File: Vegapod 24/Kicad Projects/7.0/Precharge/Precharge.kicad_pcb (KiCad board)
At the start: 2 copper layers, 92.5 x 97 mm, 53 parts, among them J1 VCU, J2 E-Stop, J3 LV Supply, J4 Intertial Switch, J5 Contactor1, J6 DCV, J7 Contactor2, J8 24V IN, K1 Relay_SPDT, K2 Relay_SPDT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

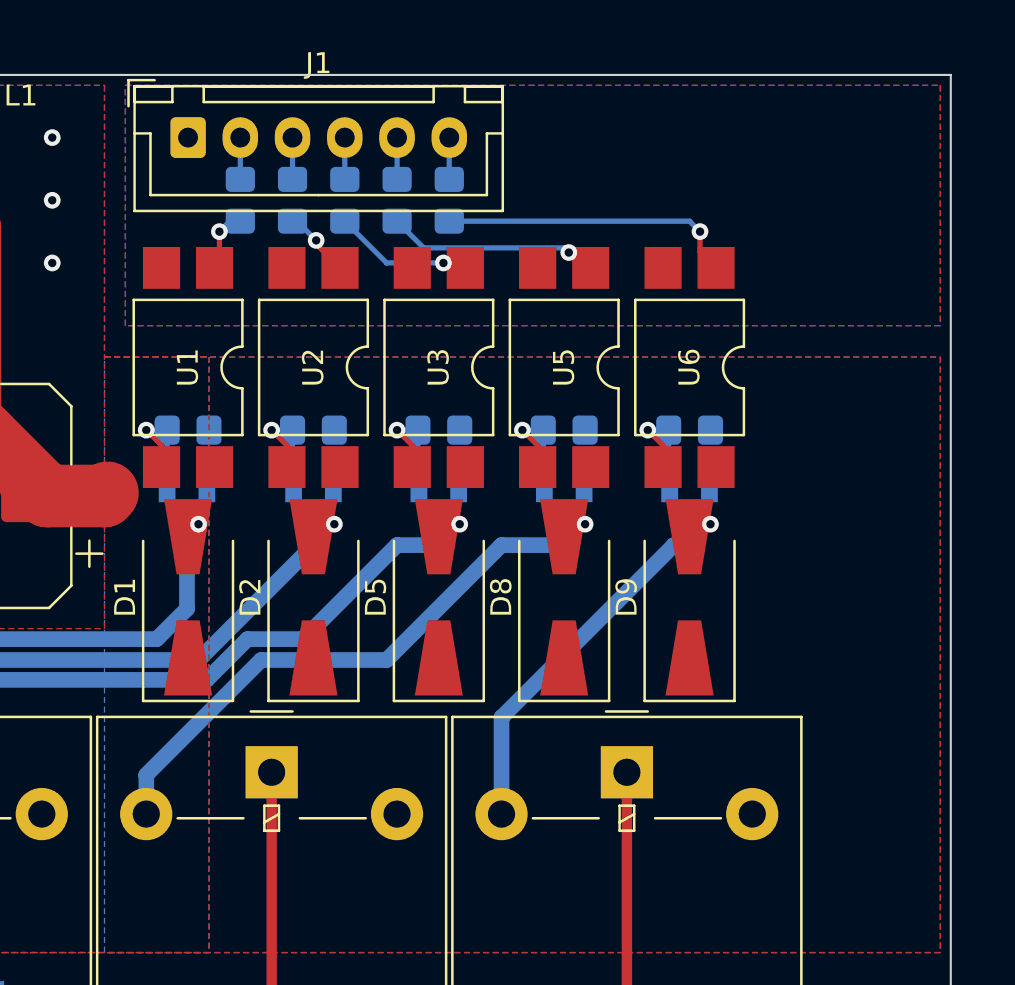
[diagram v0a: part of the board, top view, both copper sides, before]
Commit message: Added IMD Support to interlock
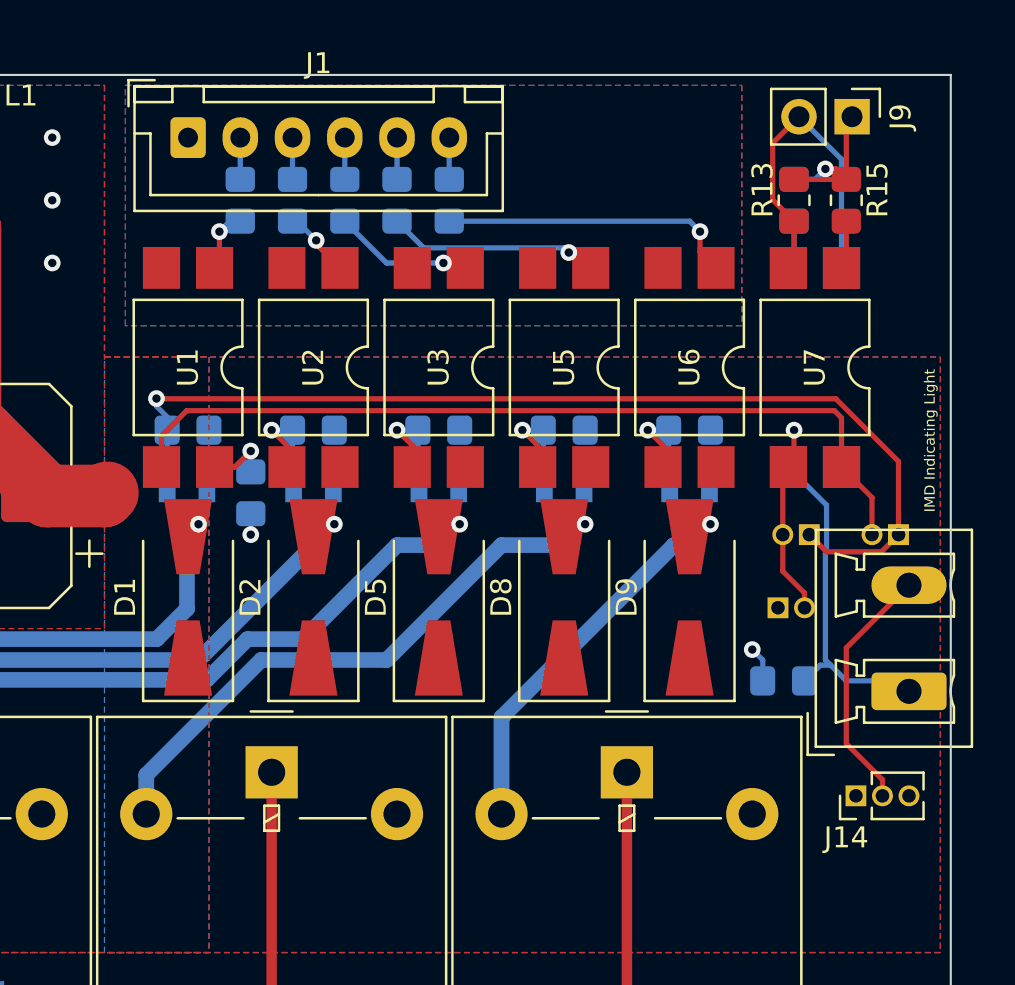
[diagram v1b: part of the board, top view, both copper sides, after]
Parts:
- added J10: ISO165Jumper, Connector_PinHeader_1.27mm:PinHeader_1x02_P1.27mm_Vertical, B.Cu at (127.0, 35.0)
- added J11: ISO165Jumper, Connector_PinHeader_1.27mm:PinHeader_1x02_P1.27mm_Vertical, B.Cu at (121.2, 38.5)
- added J12: ISO165Jumper(when OUTPUT is OK HIGH), Connector_PinHeader_1.27mm:PinHeader_1x02_P1.27mm_Vertical, B.Cu at (122.7, 35.0)
- added J13: IMD Indicating Light, Connector_Phoenix_MC_HighVoltage:PhoenixContact_MCV_1,5_2-G-5.08_1x02_P5.08mm_Vertical, F.Cu at (127.5, 42.5)
- added J14: Conn_01x03_Pin, Connector_PinHeader_1.27mm:PinHeader_1x03_P1.27mm_Vertical, F.Cu at (125.0, 47.5)
- added J9: IMD, Connector_PinHeader_2.54mm:PinHeader_1x02_P2.54mm_Vertical, F.Cu at (124.8, 15.0)
- added R13: 1000, Resistor_SMD:R_0805_2012Metric_Pad1.20x1.40mm_HandSolder, F.Cu at (124.5, 19.0)
- added R14: 1k, Resistor_SMD:R_0805_2012Metric_Pad1.20x1.40mm_HandSolder, B.Cu at (96.0, 33.0)
- added R15: 2.2k, Resistor_SMD:R_0805_2012Metric_Pad1.20x1.40mm_HandSolder, F.Cu at (122.0, 19.0)
- added R16: 1000, Resistor_SMD:R_0805_2012Metric_Pad1.20x1.40mm_HandSolder, B.Cu at (122.0, 19.0)
- added R17: 1000, Resistor_SMD:R_0805_2012Metric_Pad1.20x1.40mm_HandSolder, B.Cu at (121.5, 42.0)
- added U7: EL814, Package_DIP:SMDIP-4_W9.53mm, F.Cu at (123.0, 27.0)
- added U8: EL814, Package_DIP:SMDIP-4_W9.53mm, B.Cu at (123.0, 27.0)
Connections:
- Q1 pad 1: Net-(Q1-B) -> Net-(J10-Pin_1)
- R2 pad 2: Net-(Q1-B) -> Net-(J10-Pin_1)
- U1 pad 3: Net-(Q1-B) -> Net-(J10-Pin_2)
- U1 pad 4: +12V -> Net-(R14-Pad1)
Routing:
- net Net-(J10-Pin_1): track 0.00 -> 49.3 mm, vias 0 -> 1
- net Net-(J10-Pin_2): track 0.00 -> 40.4 mm
- net Net-(J9-Pin_2): track 0.00 -> 16.4 mm
- net Net-(J13-Pin_1): track 0.00 -> 16.2 mm
- net Net-(J13-Pin_2): track 0.00 -> 12.0 mm
- net Net-(J11-Pin_2): track 0.00 -> 9.15 mm, vias 0 -> 1
- net Net-(J9-Pin_1): track 0.00 -> 8.53 mm, vias 0 -> 1
- net Net-(Q1-B): track 5.57 -> 0.00 mm, vias 1 -> 0
- net Net-(R14-Pad1): track 0.00 -> 3.05 mm, vias 0 -> 1
- net +12V: track 43.1 -> 45.8 mm, vias 2 -> 4
- net Net-(R16-Pad1): track 0.00 -> 2.35 mm
- net Net-(R13-Pad1): track 0.00 -> 2.33 mm

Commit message: Added vegapod logo to Interlock
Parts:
- added G***: LOGO, Logo:vegapod_logo, F.Cu at (52.5, 34.5)
- added G***: LOGO, Logo:Designed by Saksham, F.Cu at (124.5, 78.5)
